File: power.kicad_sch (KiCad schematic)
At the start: 19 parts, among them J2 SATA_Power_Connector, U2 EUP3458

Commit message: rev-7 ready
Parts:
- removed LOGO1: Logo_Open_Hardware_Small, Symbol:OSHW-Logo2_9.8x8mm_SilkScreen, symbol Graphic:Logo_Open_Hardware_Small
- L1: footprint Inductor_SMD:L_0805_2012Metric -> Inductor_SMD:L_0603_1608Metric
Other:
- moved on the sheet: C12, C13, C14, C15, C16, C17, C18, D1, F1, F2, FB1, J2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

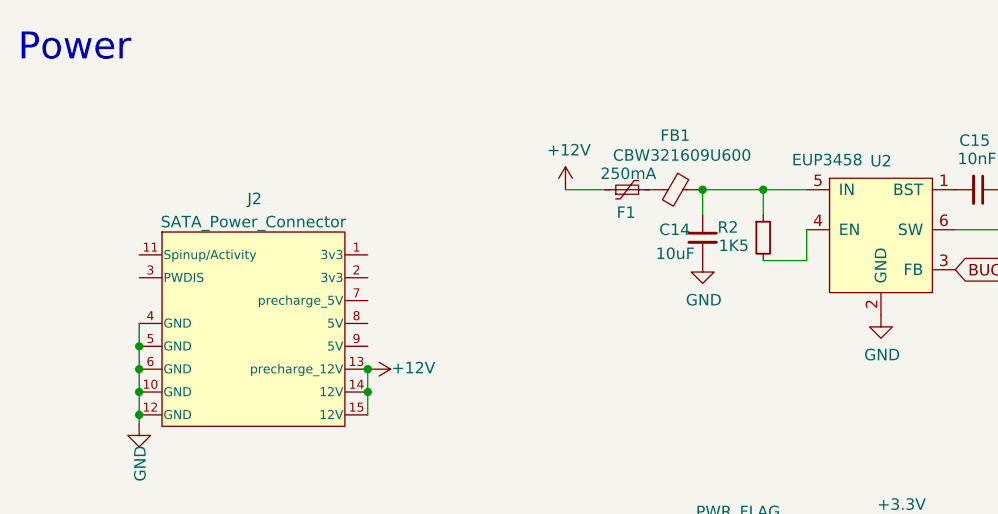
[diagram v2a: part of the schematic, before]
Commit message: wip migrate to kicad 7
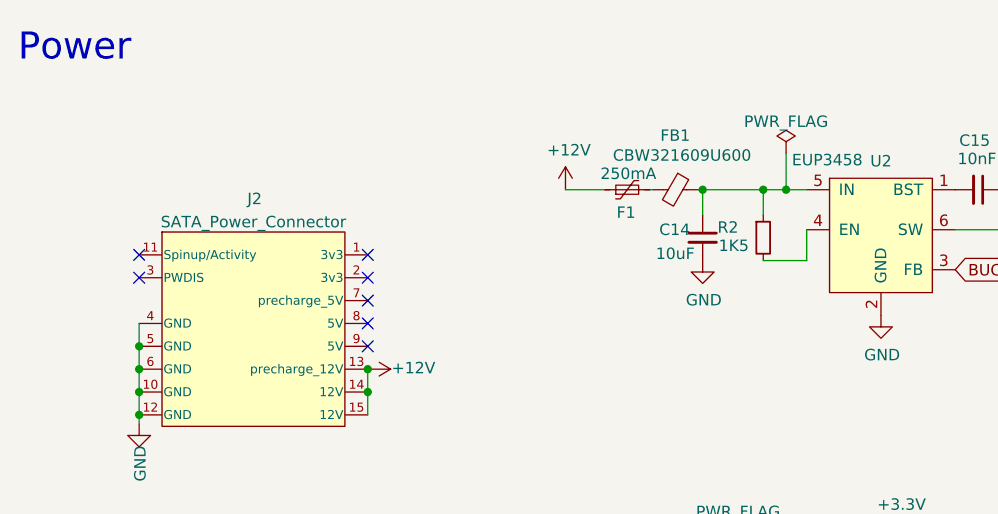
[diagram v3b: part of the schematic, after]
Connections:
- no-connect marks 0 -> 7
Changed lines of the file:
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@@
   (junction (at 128.903 35.687) (diameter 0) (color 0 0 0 0)
   )
+  (junction (at 97.79 31.242) (diameter 0) (color 0 0 0 0)
+  )
   (junction (at 97.282 75.692) (diameter 0) (color 0 0 0 0)
   )
@@
   (junction (at 25.908 56.261) (diameter 0) (color 0 0 0 0)
   )
+  (no_connect (at 25.908 38.481))
+  (no_connect (at 25.908 41.021))
+  (no_connect (at 51.308 41.021))
+  (no_connect (at 51.308 38.481))
+  (no_connect (at 51.308 48.641))
+  (no_connect (at 51.308 46.101))
+  (no_connect (at 51.308 43.561))
   (wire (pts (xy 97.282 75.692) (xy 101.981 75.692))
     (stroke (width 0) (type default))
@@
     (stroke (width 0) (type default))
   )
-  (wire (pts (xy 95.25 31.242) (xy 100.076 31.242))
+  (wire (pts (xy 95.25 31.242) (xy 97.79 31.242))
     (stroke (width 0) (type default))
   )
@@
     (stroke (width 0) (type default))
   )
+  (wire (pts (xy 97.79 31.242) (xy 100.076 31.242))
+    (stroke (width 0) (type default))
+  )
   (wire (pts (xy 51.308 51.181) (xy 51.308 53.721))
     (stroke (width 0) (type default))
@@
   )
   (wire (pts (xy 155.829 72.39) (xy 159.512 72.39))
+    (stroke (width 0) (type default))
+  )
+  (wire (pts (xy 97.79 27.178) (xy 97.79 31.242))
     (stroke (width 0) (type default))
   )
@@
         )
       )
+    )
+  )
+  (symbol (lib_id "power:PWR_FLAG") (at 97.79 27.178 0) (unit 1)
+    (in_bom yes) (on_board yes) (dnp no) (fields_autoplaced)
+    (property "Reference" "#FLG03" (at 97.79 25.273 0)
+      (effects (font (size 1.27 1.27)) hide)
+    )
+    (property "Value" "PWR_FLAG" (at 97.79 23.6761 0)
+      (effects (font (size 1.27 1.27)))
+    )
+    (property "Footprint" "" (at 97.79 27.178 0)
+      (effects (font (size 1.27 1.27)) hide)
+    )
+    (property "Datasheet" "~" (at 97.79 27.178 0)
+      (effects (font (size 1.27 1.27)) hide)
+    )
+    (pin "1")
+    (instances
+      (project "opilio"
+        (path "/1fd8049d-01e3-48fd-a73a-49757ed6cc50/8de2dfd4-e2ce-4b58-a73c-eb39ba707cfb"
+          (reference "#FLG03") (unit 1)
+        )
+      )
